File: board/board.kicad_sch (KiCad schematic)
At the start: 4 parts, among them J1 002_SPI, J2 012_CAN

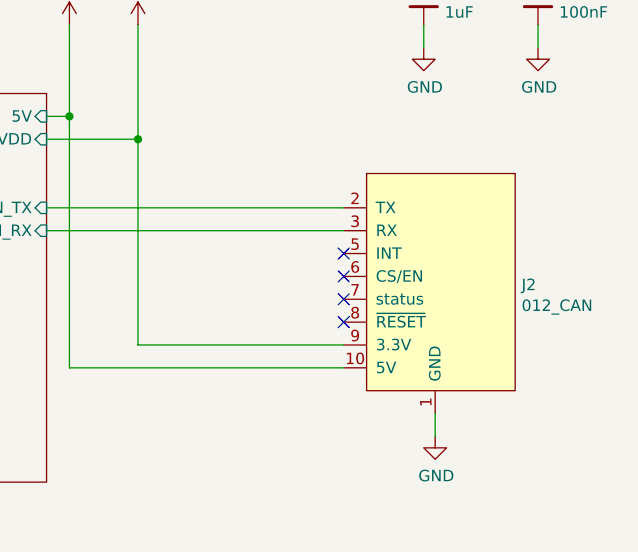
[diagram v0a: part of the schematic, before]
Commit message: updated to kicad 8.0 and 20pin tssop
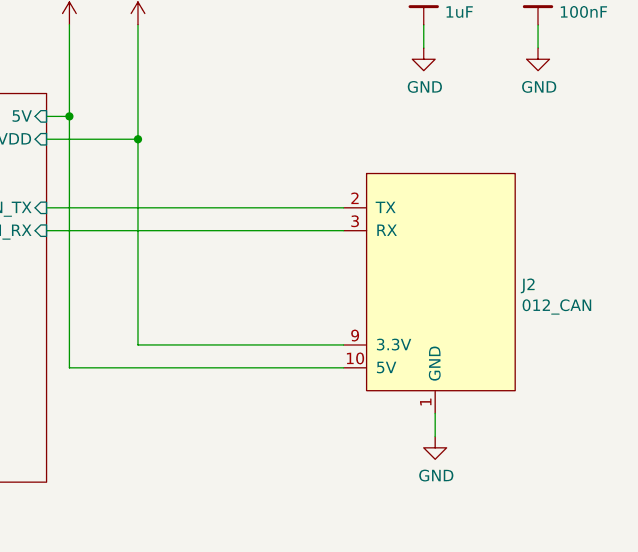
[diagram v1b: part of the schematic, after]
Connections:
- net +3V3 renamed +3.3V
- no-connect marks 4 -> 0

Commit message: added lcsc part numbers
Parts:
- C3: lcsc (none) -> C15849
- C4: lcsc (none) -> C14663
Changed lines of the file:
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@@
+      (effects (font (size 1.27 1.27)) hide)
+    )
+    (property "lcsc" "" (at 73.66 93.98 0)
       (effects (font (size 1.27 1.27)) hide)
     )
@@
       (effects (font (size 1.27 1.27)) hide)
     )
+    (property "lcsc" "" (at 193.04 96.52 0)
+      (effects (font (size 1.27 1.27)) hide)
+    )
     (pin "1")
     (pin "10")
@@
       (effects (font (size 1.27 1.27)) hide)
     )
+    (property "lcsc" "C15849" (at 191.77 66.04 0)
+      (effects (font (size 1.27 1.27)) hide)
+    )
     (pin "1")
     (pin "2")
@@
       (effects (font (size 1.27 1.27)) hide)
     )
+    (property "lcsc" "C14663" (at 204.47 66.04 0)
+      (effects (font (size 1.27 1.27)) hide)
+    )
